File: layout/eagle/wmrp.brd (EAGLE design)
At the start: 95 x 100 mm, 132 parts, among them IC1 ACS712, IC2 ADR392, IC3 ATMEGA32U4TQFP-44, IC4 AD8552, IC5 AD8552, Q1 BC817-40, Q2 BC817-40, Q3 IRF7416, Q4 IRF7413, Q5 BC817-40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

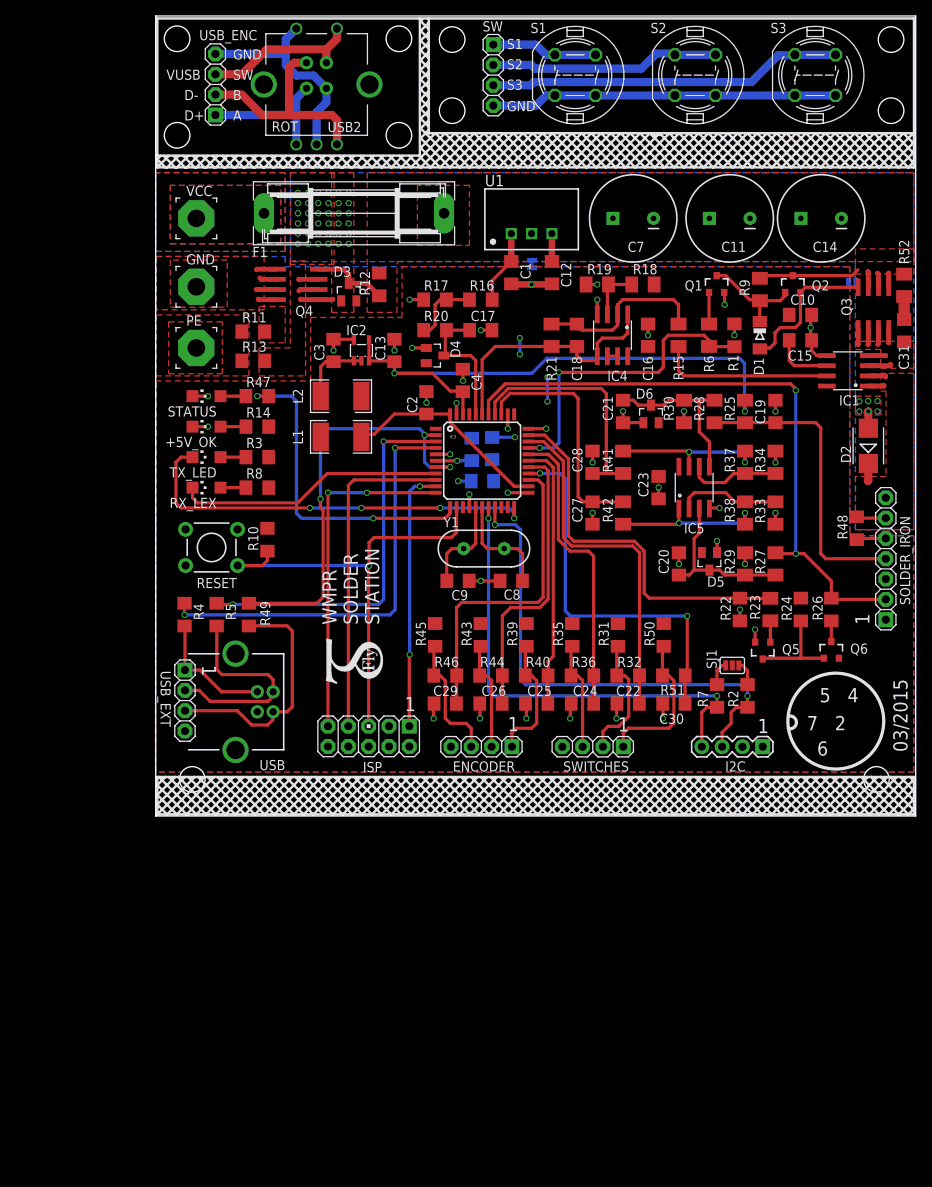
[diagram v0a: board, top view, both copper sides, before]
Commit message: Added SPI header and resistors to schematic, added SC and BL pin, moved RX_LED from pin 8 to 1
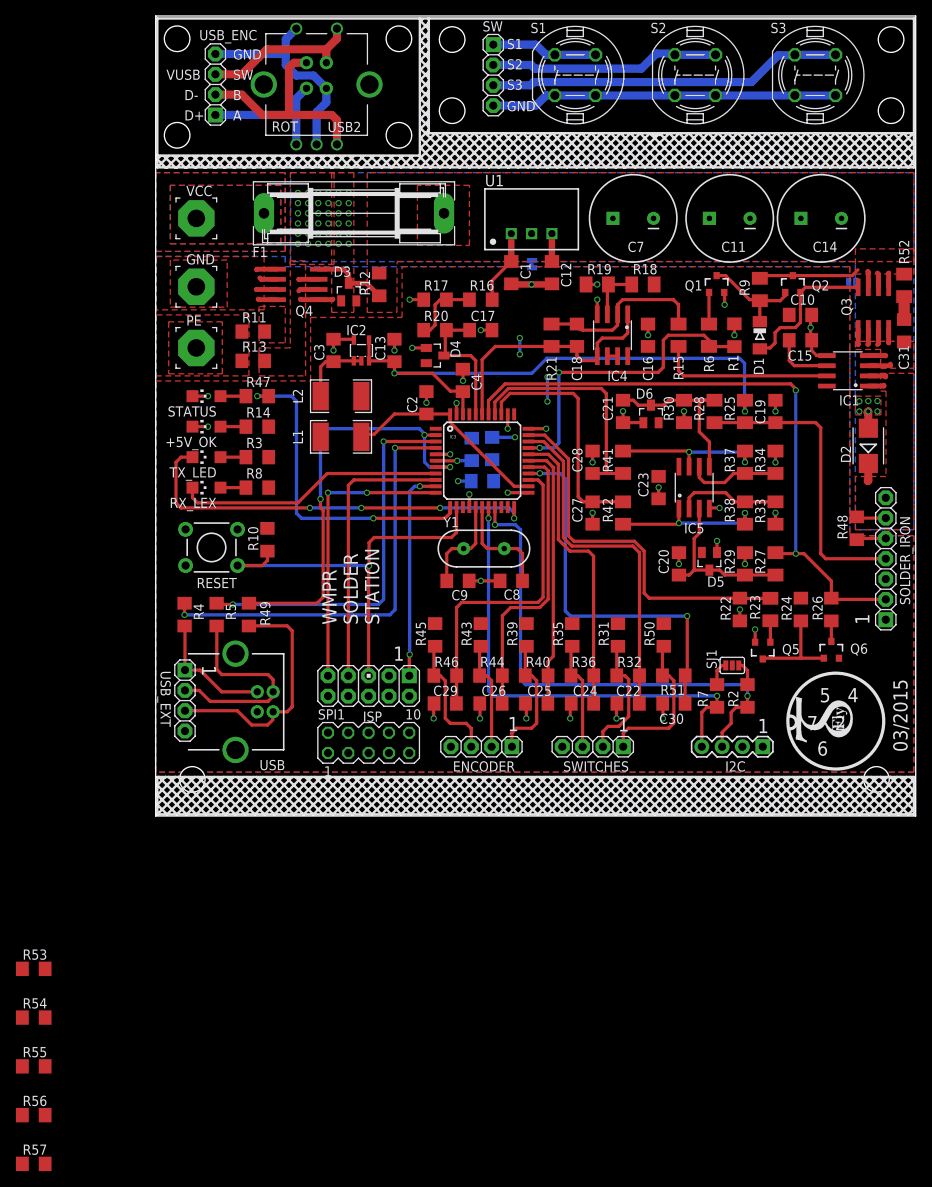
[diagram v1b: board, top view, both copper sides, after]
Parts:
- added R53, R54, R55, R56, R57: 1k, resistor:R1206
- added SPI1: (no value), con-lstb:MA05-2
- moved U$1 59.2 mm to (87.3, 8.33)
- moved ISP 6.30 mm to (26.6, 16.3)
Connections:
- new net BL: IC3.41, SPI1.2
- new net CS: IC3.8, R56.2
- new net DC: R55.2
- new net N$35: R53.1, SPI1.4
- new net N$36: R54.1, SPI1.5
- new net N$37: R55.1, SPI1.6
- new net N$38: R56.1, SPI1.7
- new net N$40: R57.1, SPI1.8
- net +5V: now also R57.2, SPI1.3
- net GND: now also SPI1.1
- net MOSI: now also R54.2
- net RX_LED: now also IC3.1; no longer IC3.8
- net SCK: now also R53.2
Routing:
- net SCK: track 41.3 -> 35.0 mm
- net RESET: track 59.2 -> 52.9 mm
- net MISO: track 42.7 -> 36.4 mm
- net MOSI: track 32.9 -> 26.6 mm

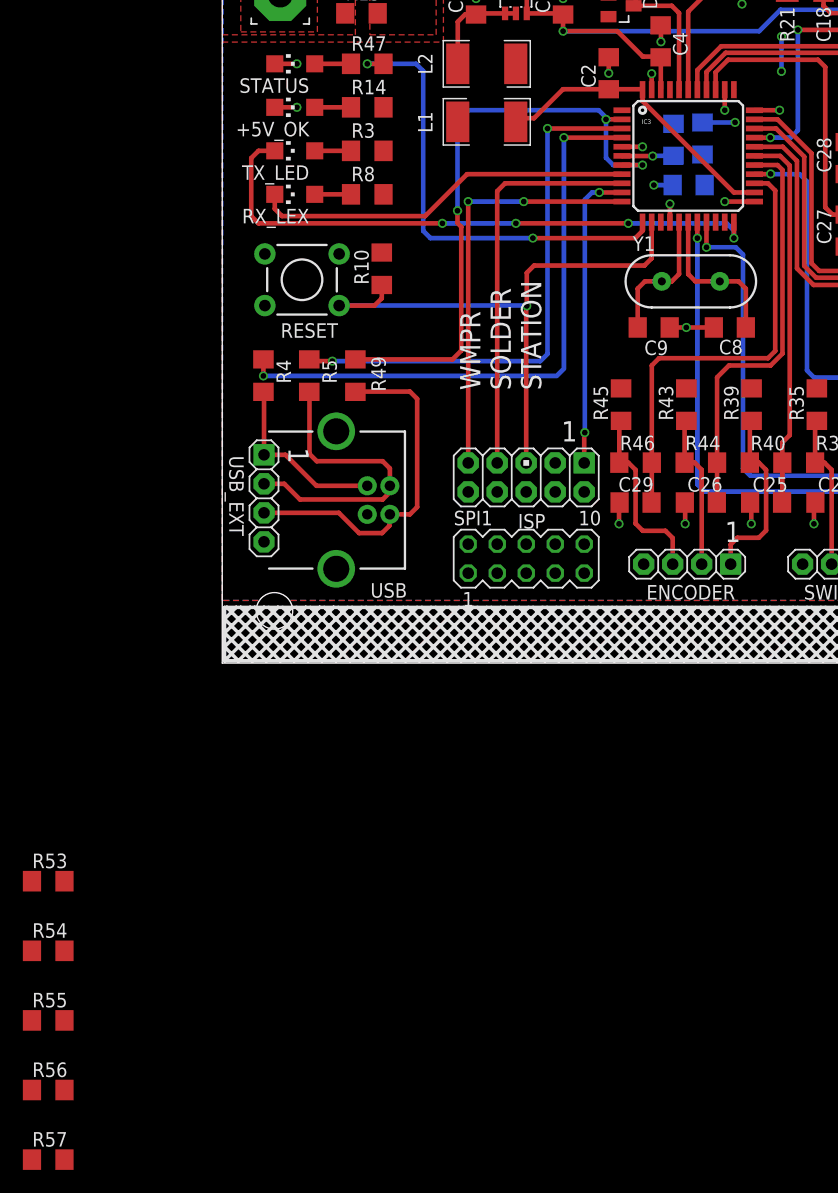
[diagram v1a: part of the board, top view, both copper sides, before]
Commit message: Added SPI header with resistors to schematic and made connections on PCB
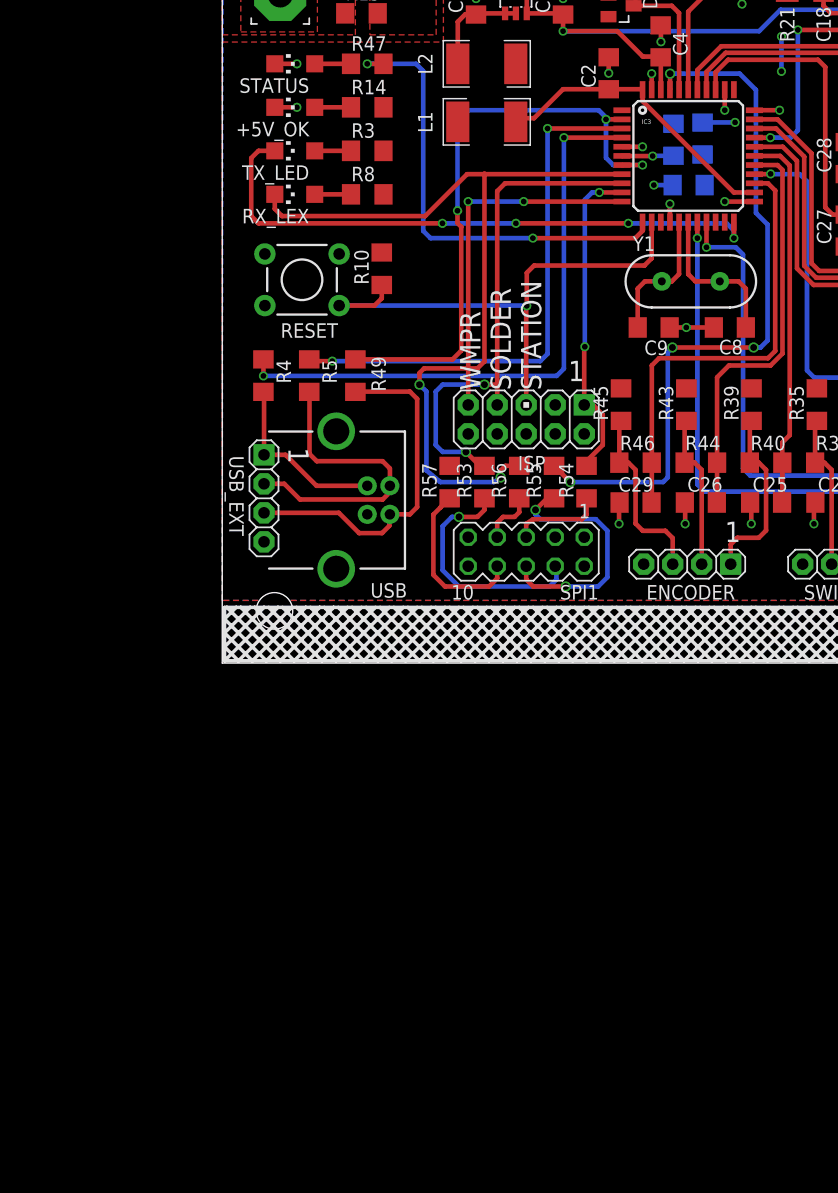
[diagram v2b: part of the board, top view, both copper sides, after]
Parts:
- moved R57 69.0 mm to (19.9, 15.8), turned to 90 degrees
- moved R56 67.3 mm to (26.0, 15.8), turned to 90 degrees
- moved R55 64.7 mm to (29.1, 15.8), turned to 90 degrees
- moved R54 62.5 mm to (31.9, 15.8), turned to 90 degrees
- moved R53 51.8 mm to (23.0, 15.8), turned to 90 degrees
- moved ISP 5.08 mm to (26.6, 21.3)
- moved SPI1 0.61 mm to (26.6, 9.75), turned to 180 degrees
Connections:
- net BL: no longer IC3.41
- net DC: now also IC3.41
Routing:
- net DC: track 0.00 -> 62.7 mm, vias 0 -> 4
- net CS: track 0.00 -> 40.8 mm, vias 0 -> 2
- net N$37: track 0.00 -> 22.3 mm, vias 0 -> 2
- net N$35: track 0.00 -> 21.1 mm, vias 0 -> 1
- net N$40: track 0.00 -> 14.7 mm
- net SCK: track 35.0 -> 45.3 mm, vias 0 -> 2
- net N$36: track 0.00 -> 8.17 mm
- net RESET: track 52.9 -> 47.8 mm
- net MISO: track 36.4 -> 31.3 mm
- net N$38: track 0.00 -> 4.80 mm
- net MOSI: track 26.6 -> 28.5 mm
